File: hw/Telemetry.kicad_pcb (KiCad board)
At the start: 4 copper layers, 100 x 82 mm, 132 parts, among them J101 BOOT0, J102 BOOT0, J103 SPORT, J104 SBUS, J105 USB_B_Micro, J106 UART_EXP, J201 Conn_01x02, J301 Conn_01x02, J302 Conn_01x02, J401 Conn_01x02, J402 Conn_01x02, J403 Conn_01x02, J404 Conn_01x02, J405 Conn_01x02, J406 Conn_01x02, J407 Conn_01x02, J408 Conn_01x02, J409 SERVO_OUT, J410 AUDIO, Q201 AO3401A, Q202 AO3401A, Q203 IRLML6344TRPBF, Q204 IRLML6344TRPBF, Q401 IRLML6344TRPBF, Q402 IRLML6344TRPBF, Q403 IRLML6344TRPBF, Q404 CSD17306Q5A, Q406 IRLML6344TRPBF, Q408 CSD17306Q5A, SW101 SW_Push, U101 STM32F303CBx, U102 IS25LP032D, U201 AP1501-K5, U202 RT6200, U301 LP2985-5.0, U302 ACS770xCB-100U-PSF, U303 MCP6001-OT, U304 ACS770xCB-100U-PSF, U305 MCP6001-OT, U401 MCP1416, U402 MCP1416, U403 AD5160BRJZ10-R2, U404 MCP6001-OT, U405 TLP2361_TPL_E, U406 TLP2361_TPL_E, X101 SG-310_SCF_8.000000MHZ

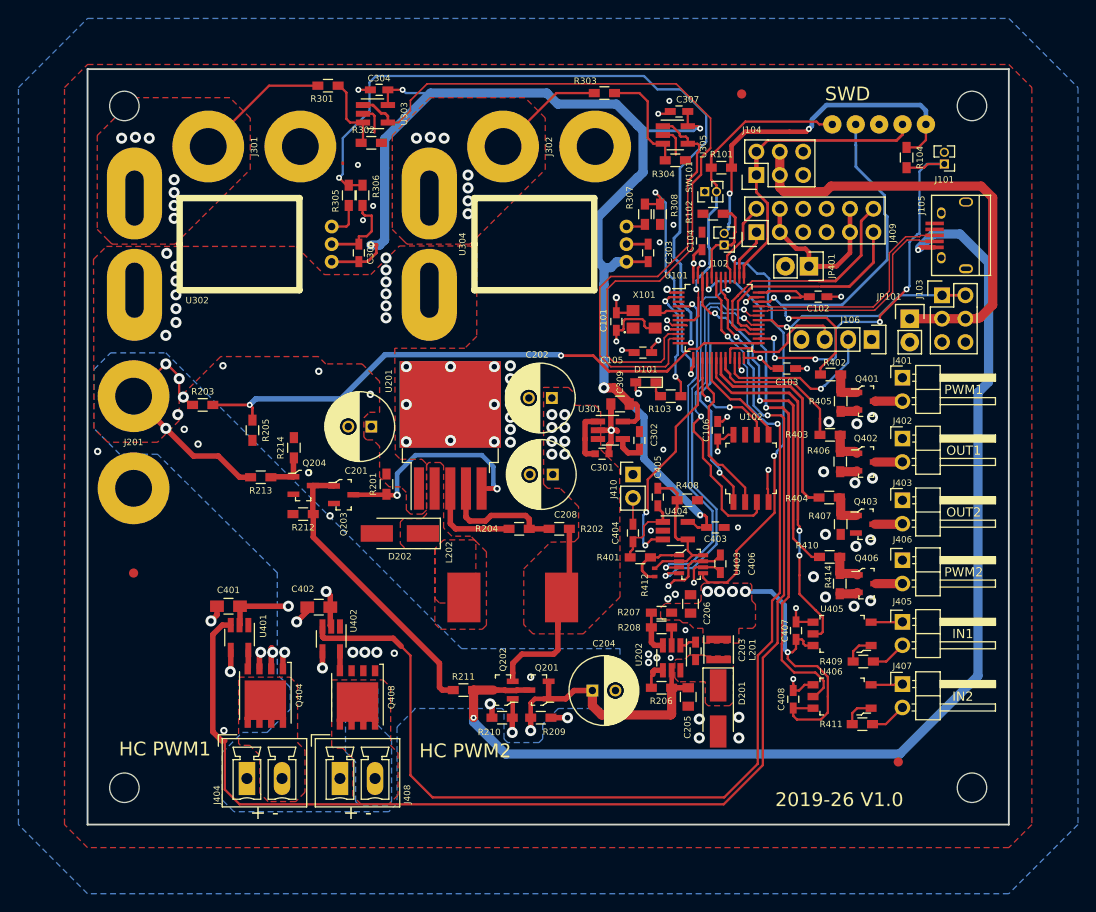
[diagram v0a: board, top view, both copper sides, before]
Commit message: Updates to board revision 0.2 and newer HAL version
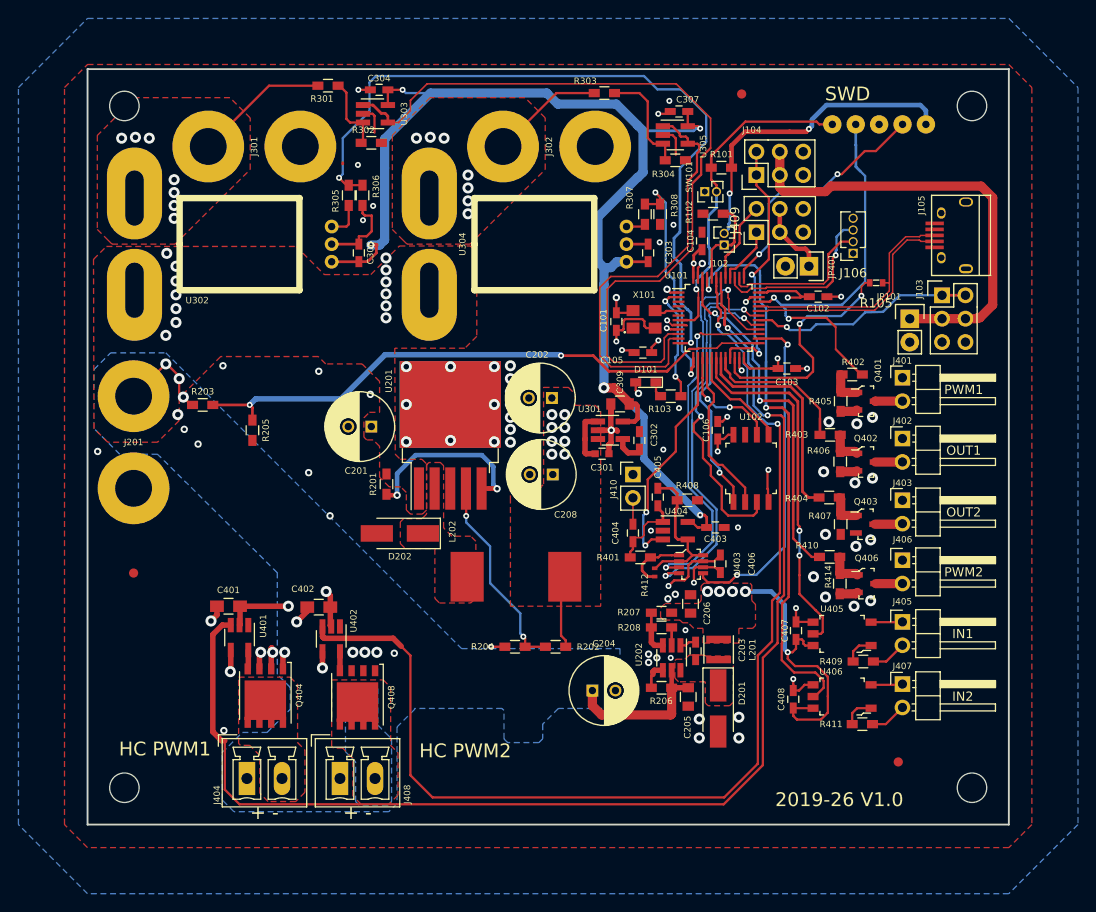
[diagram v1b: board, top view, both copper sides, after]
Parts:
- removed J101: BOOT0, Pin_Headers:Pin_Header_Straight_1x02_Pitch1.27mm
- removed Q201, Q202: AO3401A, digikey-footprints:SOT-23-3
- removed Q203, Q204: IRLML6344TRPBF, digikey-footprints:SOT-23-3
- removed R104, R211, R213: 10k, Resistors_SMD:R_0603_HandSoldering
- removed R209, R210, R212, R214: 100k, Resistors_SMD:R_0603_HandSoldering
- added R105: 1k5, digikey-footprints:0603, F.Cu at (145.6, 61.2)
- J106: footprint Pin_Headers:Pin_Header_Straight_1x04 -> Connector_PinSocket_1.27mm:PinSocket_1x04_P1.27mm_Vertical
- J409: value SERVO_OUT -> ServoCon; footprint Pin_Headers:Pin_Header_Straight_2x06 -> Connector_PinHeader_2.54mm:PinHeader_2x03_P2.54mm_Vertical
- moved R204 12.8 mm to (106.4, 100.7)
- moved R202 12.8 mm to (110.8, 100.7)
- moved J106 9.56 mm to (143.1, 58.0), turned to 180 degrees
- moved R402 2.35 mm to (143.0, 71.2), turned to 0 degrees
- moved L202 2.28 mm to (106.5, 93.1)
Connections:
- J105 pad 4: (no net) -> Net-(J105-Pad4)
- J106 pad 2: /UART_RX -> UART_RX
- J106 pad 3: /UART_TX -> UART_TX
- J409 pad 3: Net-(J409-Pad10) -> Net-(J409-Pad3)
- J409 pad 4: Net-(J409-Pad10) -> Net-(J409-Pad3)
- JP401 pad 1: Net-(J409-Pad10) -> Net-(J409-Pad3)
- TP103 pad 1: /Sbus -> Net-(TP103-Pad1)
- U101 pad 21: /UART_TX -> /Sbus
- U101 pad 22: /UART_RX -> USB_ENUMRATION
- U101 pad 26: COOLING_TEMP -> AMP_CLK
- U101 pad 27: SERVO_4 -> AMP_CS
- U101 pad 28: SERVO_3 -> AMP_DIN
- U101 pad 3: (no net) -> Net-(U101-Pad3)
- U101 pad 37: /Sbus -> Net-(TP103-Pad1)
- U101 pad 38: SERVO_1 -> UART_RX
- U101 pad 39: AMP_CLK -> UART_TX
- U101 pad 4: AMP_CS -> Net-(U101-Pad4)
- U101 pad 40: SERVO_2 -> SERVO_1
- U101 pad 41: AMP_DIN -> SERVO_2
- U101 pad 6: (no net) -> Net-(U101-Pad6)
- U102 pad 7: (no net) -> Net-(U102-Pad7)
- U401 pad 1: (no net) -> Net-(U401-Pad1)
- U402 pad 1: (no net) -> Net-(U402-Pad1)
- X101 pad 1: (no net) -> Net-(X101-Pad1)
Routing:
- net VBUS: track 125.9 -> 0.00 mm, vias 2 -> 0
- net COOLING_TEMP: track 44.9 -> 0.00 mm, vias 5 -> 0
- net +BATT: track 71.5 -> 39.4 mm, vias 22 -> 19
- net Net-(Q203-Pad1): track 31.5 -> 0.00 mm
- net SERVO_4: track 27.5 -> 0.00 mm
- net Net-(TP103-Pad1): track 0.00 -> 27.2 mm, vias 0 -> 2
- net USB_ENUMRATION: track 0.00 -> 26.4 mm, vias 0 -> 2
- net SERVO_3: track 24.6 -> 0.00 mm
- net Net-(J409-Pad10): track 20.4 -> 0.00 mm
- net UART_TX: track 0.00 -> 19.3 mm, vias 0 -> 1
- net /UART_RX: track 18.4 -> 0.00 mm, vias 1 -> 0
- net UART_RX: track 0.00 -> 16.8 mm
- net VCC: track 38.2 -> 21.5 mm
- net /UART_TX: track 14.5 -> 0.00 mm
- net GND: track 102.7 -> 90.4 mm, vias 88 -> 86
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
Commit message: Pin remapping and layout improvements
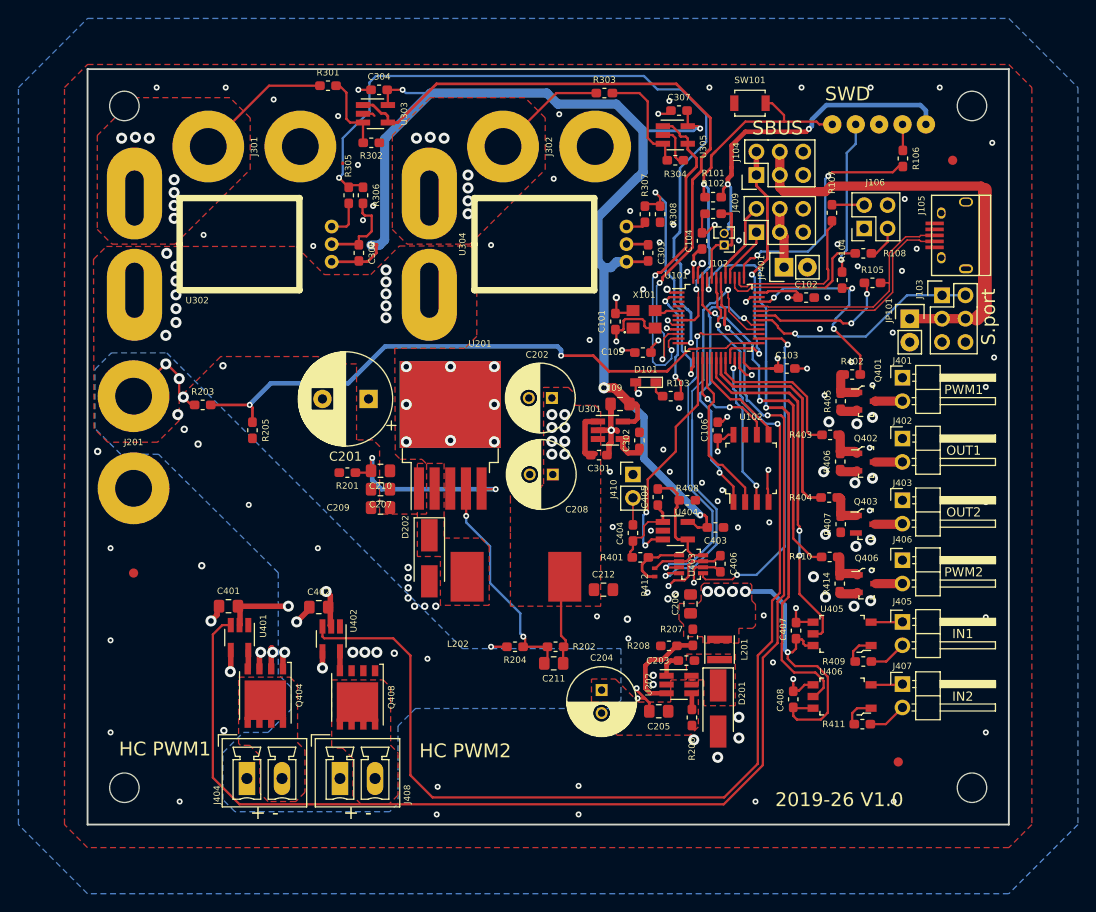
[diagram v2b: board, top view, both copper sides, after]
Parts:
- added C207: 100n, Capacitor_SMD:C_0805_2012Metric_Pad1.15x1.40mm_HandSolder, F.Cu at (91.8, 83.6)
- added C209: 10n, Capacitor_SMD:C_0805_2012Metric_Pad1.15x1.40mm_HandSolder, F.Cu at (91.8, 85.6)
- added C210: 10n, Capacitor_SMD:C_0805_2012Metric_Pad1.15x1.40mm_HandSolder, F.Cu at (91.8, 81.6)
- added C211: 100n, Capacitor_SMD:C_0805_2012Metric_Pad1.15x1.40mm_HandSolder, F.Cu at (110.6, 102.5)
- added C212: 100n, Capacitor_SMD:C_0805_2012Metric_Pad1.15x1.40mm_HandSolder, F.Cu at (116.0, 94.5)
- added R104: 50R, Resistor_SMD:R_0603_1608Metric_Pad1.05x0.95mm_HandSolder, F.Cu at (141.9, 60.9)
- added R106: 50R, Resistor_SMD:R_0603_1608Metric_Pad1.05x0.95mm_HandSolder, F.Cu at (148.5, 47.7)
- added R107: 50R, Resistor_SMD:R_0603_1608Metric_Pad1.05x0.95mm_HandSolder, F.Cu at (140.8, 53.6)
- added R108: 50R, Resistor_SMD:R_0603_1608Metric_Pad1.05x0.95mm_HandSolder, F.Cu at (144.2, 58.0)
- C101, C102, C103, C104, C105, C106, C203, C302, C303, C304, C306, C307, C403, C404, C405, C406, C407, C408: footprint Capacitors_SMD:C_0603_HandSoldering -> Capacitor_SMD:C_0603_1608Metric_Pad1.05x0.95mm_HandSolder
- C201: value 22u -> 470uF/35V; footprint Capacitors_ThroughHole:C_Radial_D7.5_L11.2_P2.5 -> Capacitor_THT:CP_Radial_D10.0mm_P5.00mm
- C202, C208: value 22u -> 100uF/10V
- C205, C206, C309: footprint Capacitors_SMD:C_0805 -> Capacitor_SMD:C_0805_2012Metric_Pad1.15x1.40mm_HandSolder
- C301: footprint Capacitors_SMD:C_0603 -> Capacitor_SMD:C_0603_1608Metric_Pad1.05x0.95mm_HandSolder
- C401, C402: footprint Capacitors_SMD:C_0805_HandSoldering -> Capacitor_SMD:C_0805_2012Metric_Pad1.15x1.40mm_HandSolder
- J106: footprint Connector_PinSocket_1.27mm:PinSocket_1x04_P1.27mm_Vertical -> Connector_PinHeader_2.54mm:PinHeader_2x02_P2.54mm_Vertical
- R101, R102, R103, R201, R202, R203, R204, R205, R206, R207, R208, R301, R302, R303, R304, R305, R306, R307, R308, R401, R402, R403, R404, R405, R406, R407, R408, R409, R410, R411, R414: footprint Resistors_SMD:R_0603_HandSoldering -> Resistor_SMD:R_0603_1608Metric_Pad1.05x0.95mm_HandSolder
- R105: footprint digikey-footprints:0603 -> Resistor_SMD:R_0603_1608Metric_Pad1.05x0.95mm_HandSolder
- SW101: footprint Pin_Headers:Pin_Header_Straight_1x02_Pitch1.27mm -> Button_Switch_SMD:SW_SPST_B3U-1000P
- moved REF** 24.0 mm to (153.9, 47.9)
- moved SW101 10.8 mm to (131.9, 41.7), turned to 0 degrees
- moved R206 4.61 mm to (125.6, 108.4), turned to 270 degrees
- moved R201 4.43 mm to (88.2, 81.8), turned to 180 degrees
- moved R207 4.33 mm to (125.7, 99.7), turned to 270 degrees
- moved D202 4.19 mm to (97.1, 91.1), turned to 270 degrees
- moved C205 3.56 mm to (122.0, 107.7), turned to 180 degrees
- moved R101 3.32 mm to (127.9, 51.9)
- moved C201 3.01 mm to (90.5, 73.8)
- moved U202 3.01 mm to (124.2, 104.8), turned to 0 degrees
- moved J106 2.95 mm to (144.3, 55.3), turned to 90 degrees
- moved JP401 2.70 mm to (135.6, 59.5), turned to 90 degrees
- moved R208 2.15 mm to (123.1, 100.6), turned to 180 degrees
- moved C203 1.45 mm to (125.0, 102.2), turned to 180 degrees
- moved C102 1.30 mm to (138.0, 62.8)
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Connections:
- J106 pad 2: UART_RX -> Net-(J106-Pad2)
- R201 pad 2: +BATT -> GND
- TP102 pad 1: PWM1 -> Net-(R104-Pad1)
- TP103 pad 1: Net-(TP103-Pad1) -> Net-(R106-Pad1)
- U101 pad 22: USB_ENUMRATION -> WP
- U101 pad 31: /WP -> USB_ENUMRATION
- U101 pad 37: Net-(TP103-Pad1) -> Net-(R106-Pad2)
- U101 pad 39: UART_TX -> Net-(R108-Pad2)
- U102 pad 3: /WP -> WP
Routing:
- net /WP: track 39.0 -> 0.00 mm, vias 2 -> 0
- net Net-(TP103-Pad1): track 27.2 -> 0.00 mm, vias 2 -> 0
- net Net-(R106-Pad2): track 0.00 -> 26.6 mm, vias 0 -> 2
- net PWM1: track 44.5 -> 23.5 mm, vias 2 -> 3
- net Net-(R108-Pad2): track 0.00 -> 17.5 mm
- net +BATT: track 39.4 -> 22.1 mm, vias 19 -> 18
- net Net-(R104-Pad1): track 0.00 -> 16.8 mm, vias 0 -> 1
- net WP: track 0.00 -> 16.8 mm, vias 0 -> 2
- net UART_TX: track 19.3 -> 3.74 mm, vias 1 -> 0
- net ESC2_VOLTAGE_OUT: track 47.4 -> 35.9 mm, vias 0 -> 2
- net USB_ENUMRATION: track 26.4 -> 15.6 mm
- net ESC1_VOLTAGE_OUT: track 86.7 -> 80.1 mm, vias 0 -> 2
- net Net-(R207-Pad2): track 4.61 -> 11.0 mm
- net Net-(R101-Pad1): track 36.3 -> 40.6 mm, vias 1 -> 2
- net Net-(J106-Pad2): track 0.00 -> 3.51 mm
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- removed copper zone on B.Cu, net Net-(J408-Pad2)
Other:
- board text added: "S.port"
- board text added: "SBUS"

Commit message: Changed High current pwm connectors to 5mm pitch versions
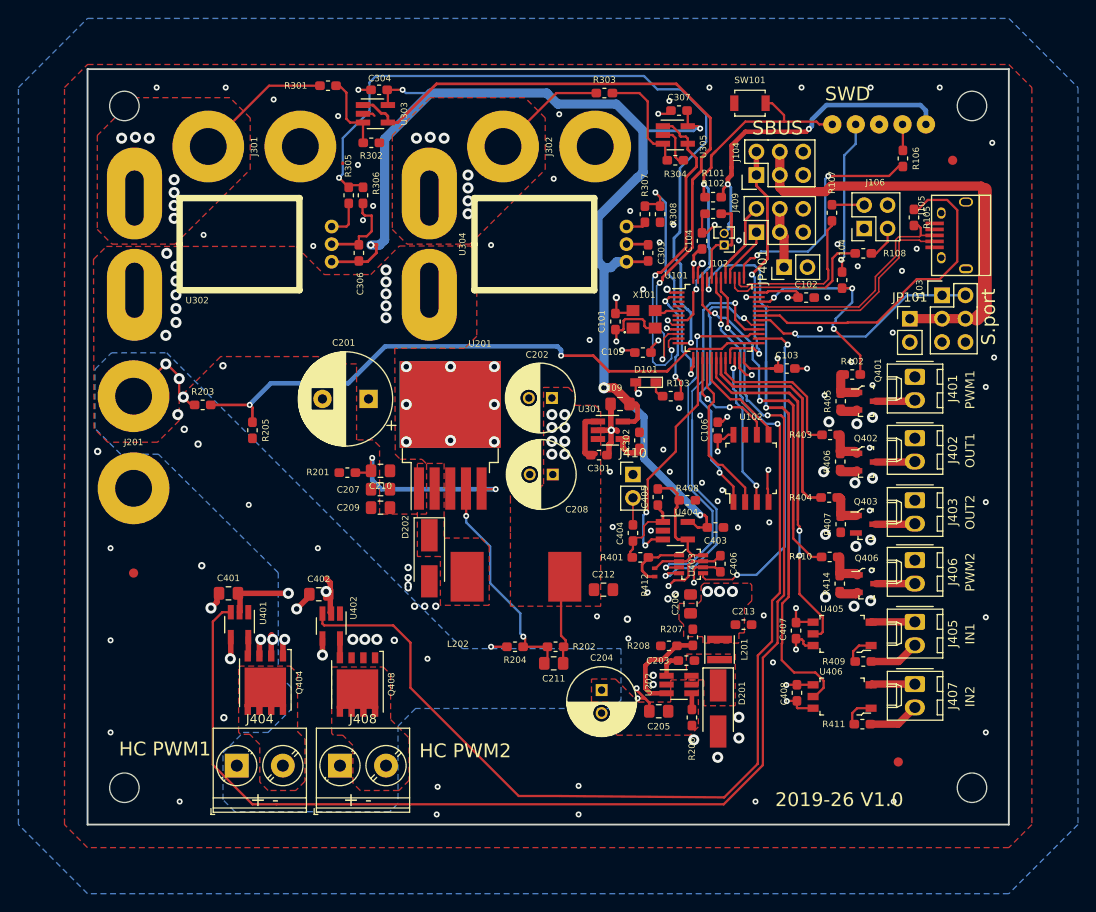
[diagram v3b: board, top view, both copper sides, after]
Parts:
- added C213: 10n, Capacitor_SMD:C_0603_1608Metric_Pad1.05x0.95mm_HandSolder, F.Cu at (131.2, 98.3)
- C206: value 2u2 -> 10u
- J401, J402, J403, J405, J406, J407: footprint Pin_Headers:Pin_Header_Angled_1x02_Pitch2.54mm -> Connector_Molex:Molex_KK-254_AE-6410-02A_1x02_P2.54mm_Vertical
- J404, J408: footprint Connectors_Phoenix:PhoenixContact_MCV-G_02x3.81mm_Vertical -> TerminalBlock_Phoenix:TerminalBlock_Phoenix_PT-1,5-2-5.0-H_1x02_P5.00mm_Horizontal
- J410: footprint Pin_Headers:Pin_Header_Straight_1x02_Pitch2.54mm -> Connector_PinHeader_2.54mm:PinHeader_1x02_P2.54mm_Vertical
- JP101, JP401: footprint Pin_Headers:Pin_Header_Straight_1x02 -> Connector_PinHeader_2.54mm:PinHeader_1x02_P2.54mm_Vertical
- moved R105 8.41 mm to (149.7, 54.1), turned to 90 degrees
- moved J404 1.78 mm to (76.2, 113.6)
- moved C402 1.40 mm to (85.1, 95.0)
- moved J408 1.40 mm to (87.4, 113.6)
- moved Q404 1.40 mm to (79.3, 104.6)
- moved Q408 1.40 mm to (89.3, 104.8)
- moved U401 1.40 mm to (76.5, 98.3)
- moved C401 1.40 mm to (75.3, 94.9)
- moved U402 1.40 mm to (86.5, 98.5)
- moved J401 1.35 mm to (149.8, 71.4), turned to 270 degrees
- moved J402 1.35 mm to (149.8, 78.1), turned to 270 degrees
- moved J403 1.35 mm to (149.8, 84.8), turned to 270 degrees
- moved J405 1.35 mm to (149.8, 98.0), turned to 270 degrees
- moved J406 1.35 mm to (149.8, 91.3), turned to 270 degrees
- moved J407 1.35 mm to (149.8, 104.8), turned to 270 degrees
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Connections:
- net /USB_D+ renamed USB_D+
- net /USB_D- renamed USB_D-
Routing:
- net +3V3: track 97.9 -> 73.5 mm
- net USB_ENUMRATION: track 15.6 -> 36.1 mm, vias 2 -> 0
- net HC_PWM2: track 122.8 -> 118.0 mm
- net GND: track 93.5 -> 91.5 mm, vias 149 -> 146
- net Net-(J407-Pad2): track 4.06 -> 5.57 mm
- net Net-(J405-Pad2): track 3.96 -> 5.45 mm
- net AMP_DIN: track 45.6 -> 44.2 mm
- net Net-(J406-Pad2): track 2.84 -> 4.20 mm
- net Net-(J405-Pad1): track 3.41 -> 4.76 mm
- net Net-(J407-Pad1): track 3.43 -> 4.78 mm
- net Net-(J401-Pad2): track 2.95 -> 4.30 mm
- net Net-(J402-Pad2): track 2.95 -> 4.27 mm
- net Net-(J403-Pad2): track 3.02 -> 4.32 mm
- net HC_PWM1: track 140.3 -> 139.2 mm
- net Net-(R101-Pad1): track 40.6 -> 40.0 mm
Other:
- net class USB added: clearance 0.2, trace_width 0.25, via_dia 0.65, via_drill 0.3

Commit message: Added connector 3D model Changed inductors to be compatible with JLCPCB smt assembly
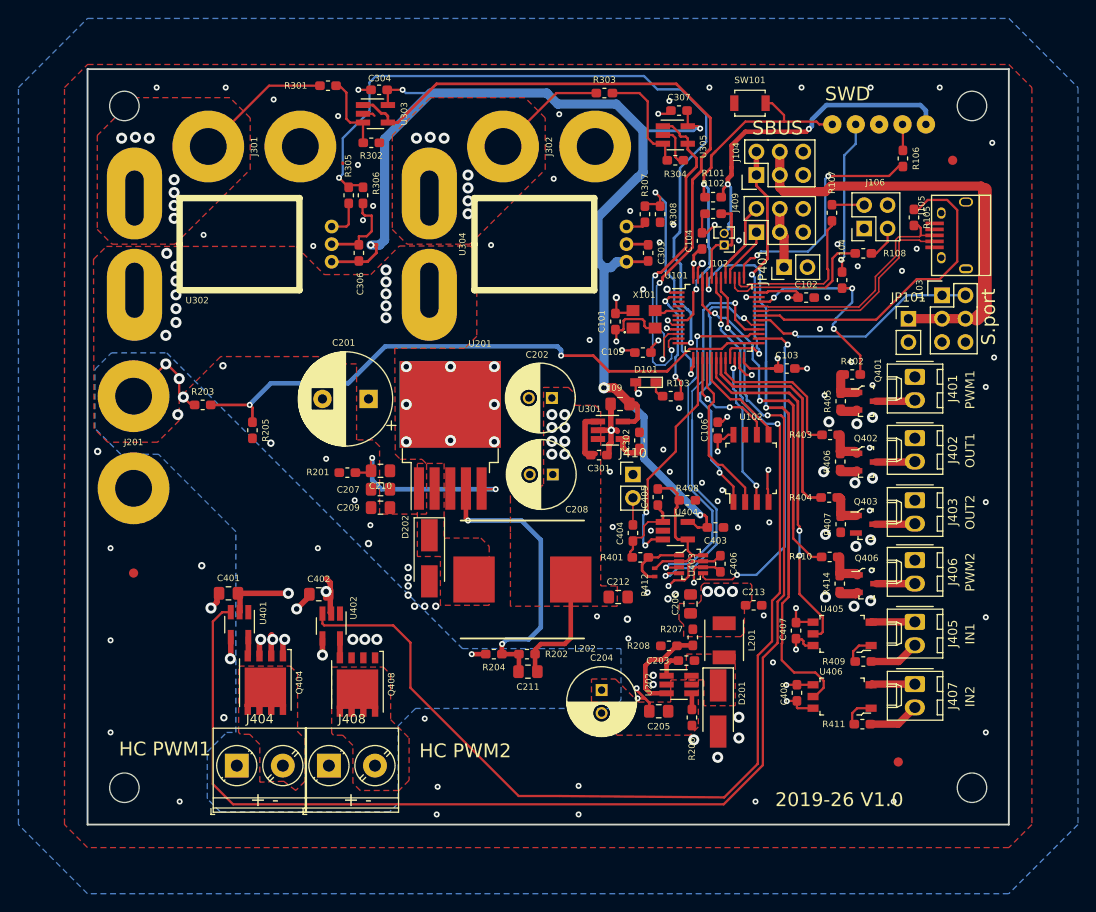
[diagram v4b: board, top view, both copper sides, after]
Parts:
- added https://github.com/findersee/rctelemetry: https://github.com/findersee/rctelemetry, PCBDecals:rctelemetry_QR, B.Cu at (128.5, 106.4)
- L201: footprint Inductors:Inductor_Taiyo-Yuden_MD-3030 -> PCBDecals:L_Sunlord_MWSA0402
- L202: footprint PCBDecals:12x12_inductor -> PCBDecals:L_Sunlord_MWSA1206
- moved R202 3.20 mm to (107.7, 101.5)
- moved C211 2.94 mm to (107.8, 103.4)
- moved R204 2.44 mm to (104.1, 101.5)
- moved C213 2.37 mm to (132.3, 96.2)
- moved C212 1.79 mm to (117.6, 95.3)
- moved J408 1.20 mm to (86.2, 113.6)
- moved L201 1.12 mm to (129.1, 100.0)
- moved L202 0.76 mm to (107.2, 93.4), turned to 0 degrees
- moved JP101 0.15 mm to (149.1, 65.1)
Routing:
- net Net-(C211-Pad2): track 24.0 -> 31.7 mm
- net VCC: track 23.3 -> 26.9 mm
- net HC_PWM1: track 139.2 -> 140.4 mm
- net USB_ENUMRATION: track 36.1 -> 35.5 mm
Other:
- board text removed: "https://github.com/findersee/rctelemetry"
